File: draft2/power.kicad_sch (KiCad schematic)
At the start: 23 parts, among them U5 LM66100, U6 LM66100, U7 MAX77827AEFD+T, U8 SC4215

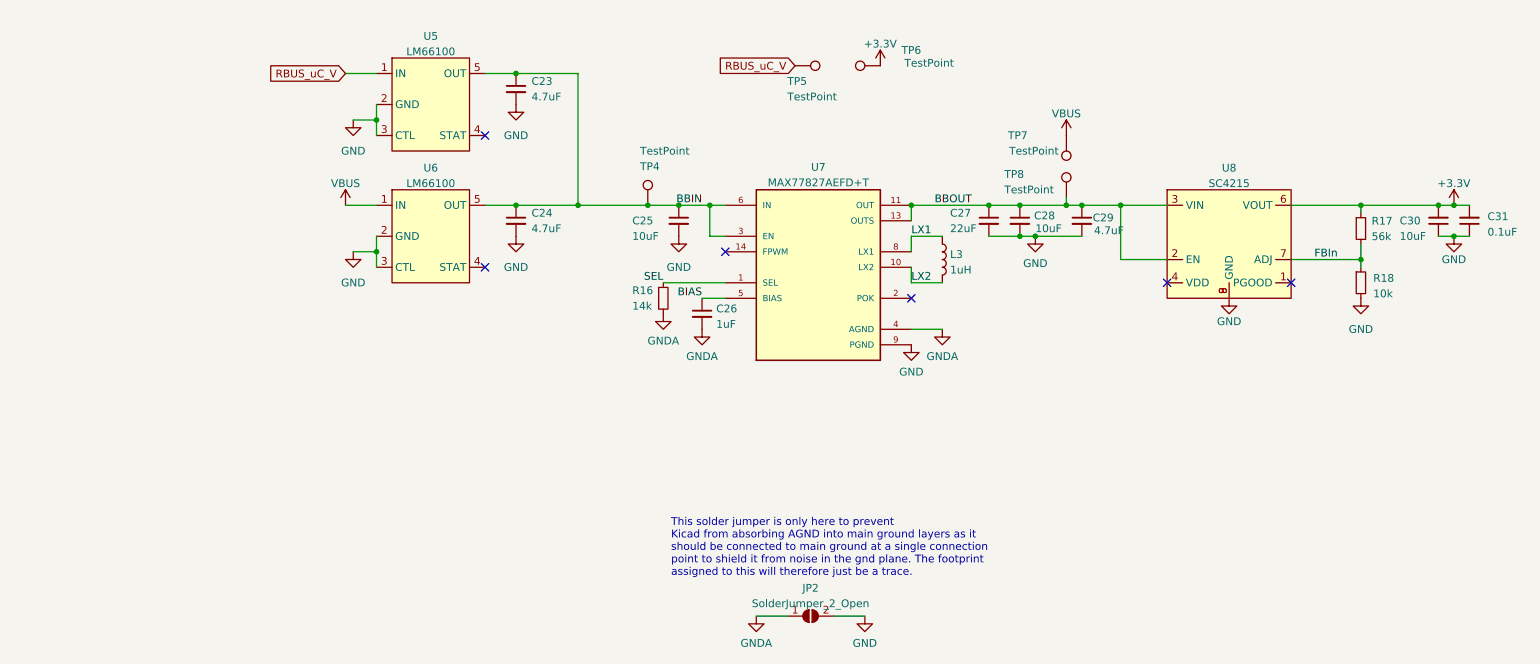
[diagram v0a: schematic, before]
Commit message: pcb roughly organized
andrei updated his board agaain
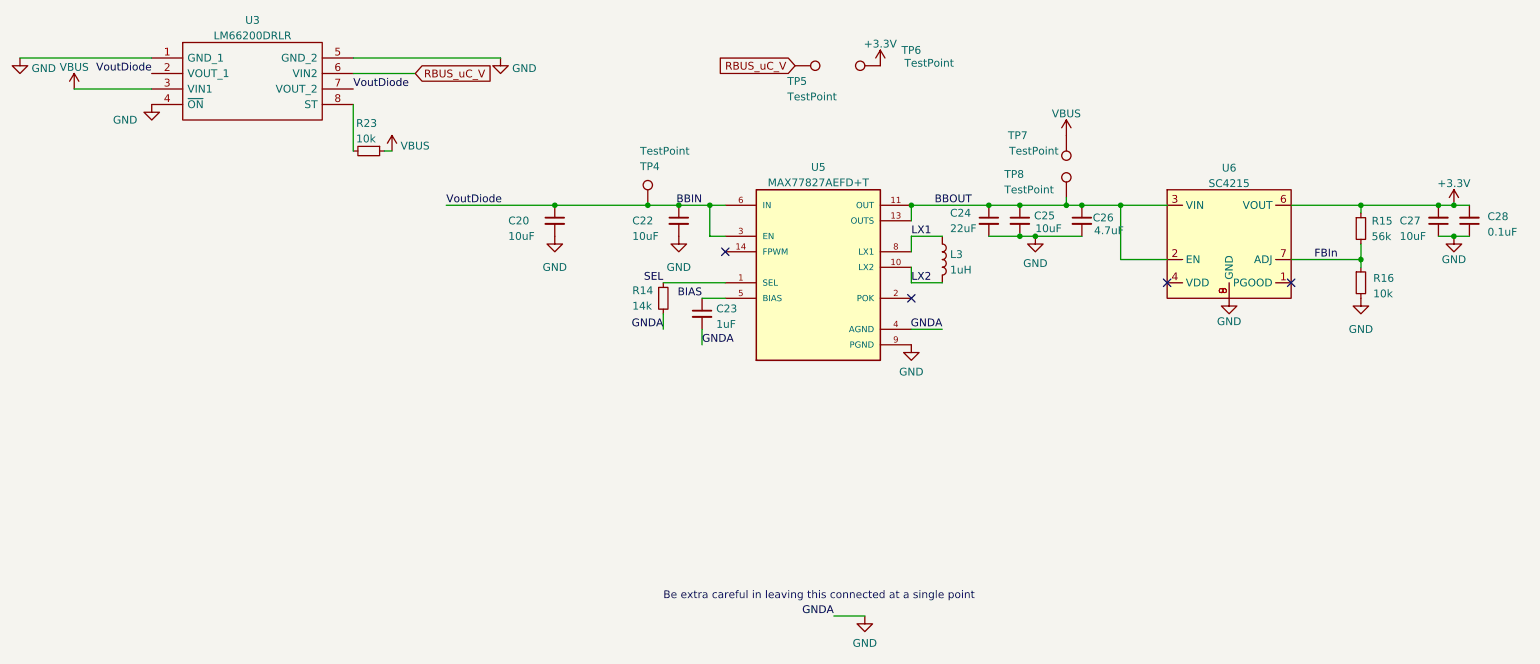
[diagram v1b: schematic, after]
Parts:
- removed C23, C24: 4.7uF, Capacitor_SMD:C_0402_1005Metric, symbol Device:C_Small
- removed JP2: SolderJumper_2_Open, symbol Jumper:SolderJumper_2_Open
- removed U5, U6: LM66100, Package_TO_SOT_SMD:SOT-23-5, symbol iclr:LTC4411
- added C20: 10uF, Capacitor_SMD:C_0402_1005Metric, symbol Device:C_Small
- added R23: 10k, Resistor_SMD:R_0402_1005Metric, symbol Device:R_Small
- added U3: LM66200DRLR, iclr:SOTFL50P160X60-8N, symbol iclr:LM66200DRLR
- renumbered C25 to C22, C26 to C23, C27 to C24, C28 to C25, C29 to C26, C30 to C27, C31 to C28, R16 to R14, R17 to R15, R18 to R16, U7 to U5, U8 to U6
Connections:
- net GNDA is gone; now on net GND: C23.2, R14.2, U5.4 (AGND)
- net BBIN: now also C20.1, U3.2 (VOUT_1), U3.7 (VOUT_2)
- net GND: now also C20.2, U3.1 (GND_1), U3.4 (~{ON}), U3.5 (GND_2)
- net RBUS_uC_V: now also U3.6 (VIN2)
- net VBUS: now also R23.1, U3.3 (VIN1)
- new net: R23.2, U3.8 (ST)
- no-connect marks 6 -> 4
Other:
- note added: "Be extra careful in leaving this connected at a single point"
- note removed: "This solder jumper is only here to prevent Kicad from absorbing AGND into main ground layers as it should be connected to main ground at a single connection point to shield it from noise in the gnd plane. The footprint assigned to this will therefore just be a trace."
